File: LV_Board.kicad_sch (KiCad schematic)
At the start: 19 parts

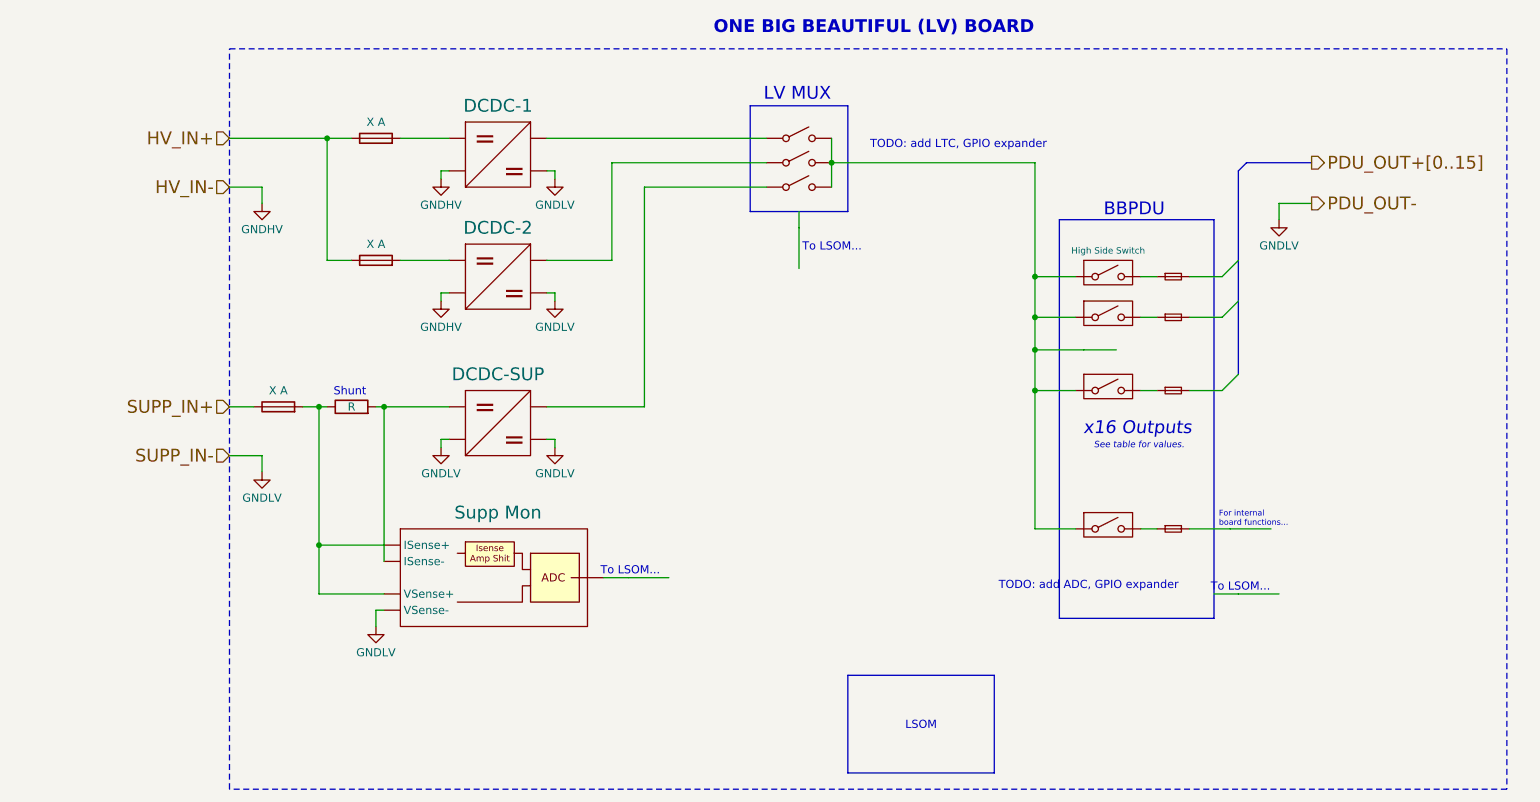
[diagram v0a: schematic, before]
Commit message: reorganized top
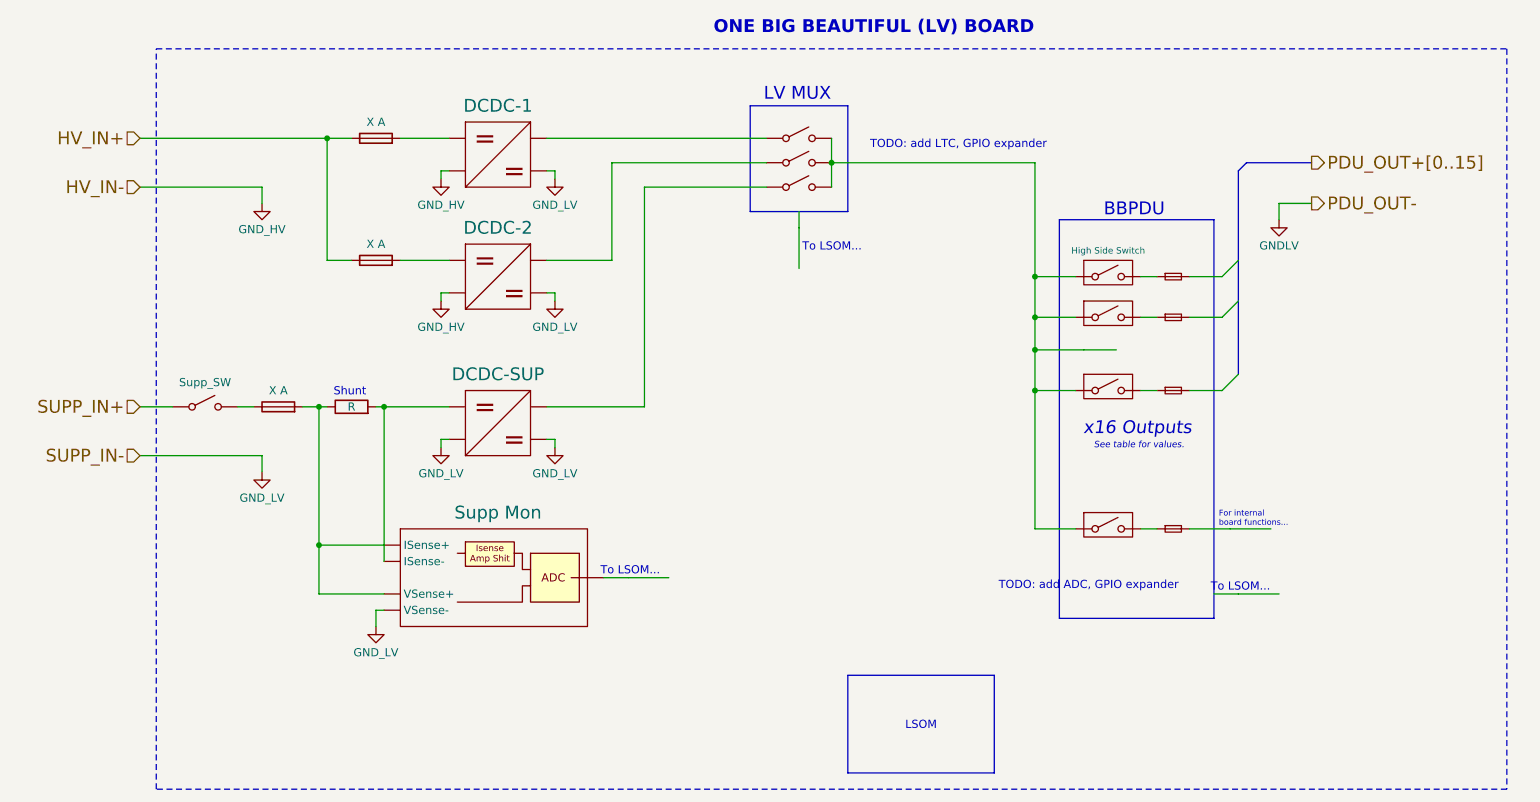
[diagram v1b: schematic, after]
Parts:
- added SW1: Supp_SW, symbol Switch:SW_SPST
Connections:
- net GNDHV is gone; now on net GND_LV: U?., U?.
- net GNDLV: no longer U?., U?., U?., U?.
- net SUPP_IN+: now also SW1. (B); no longer F?.1
- net GND_LV: now reaches U?.
- net GND_LV: now also U?.
- net at SW?. (B): now also SW?. (B), SW?. (B), U?., U?., U?., U?.; no longer U?.
- new net: R?.2, U?., U?.
- new net: SW?. (B), U?.
- new net: F?.1, SW1. (B)
- new net GND_HV: U?., U?.
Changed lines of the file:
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@@
 	(paper "A4")
 	(rectangle
-		(start 49.53 35.56)
+		(start 38.1 35.56)
 		(end 248.92 151.13)
 		(stroke
@@
 	(wire
 		(pts
-			(xy 49.53 91.44) (xy 53.34 91.44)
+			(xy 35.56 91.44) (xy 40.64 91.44)
 		)
 		(stroke
@@
 	(wire
 		(pts
-			(xy 49.53 57.15) (xy 54.61 57.15)
+			(xy 35.56 57.15) (xy 54.61 57.15)
 		)
 		(stroke
@@
 	(wire
 		(pts
+			(xy 50.8 91.44) (xy 53.34 91.44)
+		)
+		(stroke
+			(width 0)
+			(type default)
+		)
+	)
+	(wire
+		(pts
 			(xy 82.55 96.52) (xy 83.82 96.52)
 		)
@@
 	(wire
 		(pts
-			(xy 49.53 99.06) (xy 54.61 99.06)
+			(xy 35.56 99.06) (xy 54.61 99.06)
 		)
 		(stroke
@@
 	(wire
 		(pts
-			(xy 49.53 49.53) (xy 64.77 49.53)
+			(xy 35.56 49.53) (xy 64.77 49.53)
 		)
 		(stroke
@@
 			)
 		)
+		(column_widths 16.51 12.7)
+		(row_heights 2.54 2.54 2.54)
+		(cells
+			(table_cell "SIGNALS FROM"
+				(exclude_from_sim no)
+				(at 106.68 119.38 0)
+				(size 16.51 2.54)
+				(margins 0.9525 0.9525 0.9525 0.9525)
+				(span 1 1)
+				(fill
+					(type none)
+				)
+				(effects
+					(font
+						(size 1.27 1.27)
+						(thickness 0.254)
+						(bold yes)
+					)
+					(justify left top)
+				)
+			)
+			(table_cell "MEDIUM"
+				(exclude_from_sim no)
+				(at 123.19 119.38 0)
+				(size 12.7 2.54)
+				(margins 0.9525 0.9525 0.9525 0.9525)
+				(span 1 1)
+				(fill
+					(type none)
+				)
+				(effects
+					(font
+						(size 1.27 1.27)
+						(thickness 0.254)
+						(bold yes)
+					)
+					(justify left top)
+				)
+			)
+			(table_cell "VSense"
+				(exclude_from_sim no)
+				(at 106.68 121.92 0)
+				(size 16.51 2.54)
+				(margins 0.9525 0.9525 0.9525 0.9525)
+				(span 1 1)
+				(fill
+					(type none)
+				)
+				(effects
+					(font
+						(size 1 1)
+					)
+					(justify left top)
+				)
+			)
+			(table_cell "SPI ADC"
+				(exclude_from_sim no)
+				(at 123.19 121.92 0)
+				(size 12.7 2.54)
+				(margins 0.9525 0.9525 0.9525 0.9525)
+				(span 1 1)
+				(fill
+					(type none)
+				)
+				(effects
+					(font
+						(size 1 1)
+					)
+					(justify left top)
+				)
+			)
+			(table_cell "ISense"
+				(exclude_from_sim no)
+				(at 106.68 124.46 0)
+				(size 16.51 2.54)
+				(margins 0.9525 0.9525 0.9525 0.9525)
+				(span 1 1)
+				(fill
+					(type none)
+				)
+				(effects
+					(font
+						(size 1 1)
+					)
+					(justify left top)
+				)
+			)
+			(table_cell "SPI ADC"
+				(exclude_from_sim no)
+				(at 123.19 124.46 0)
+				(size 12.7 2.54)
+				(margins 0.9525 0.9525 0.9525 0.9525)
+				(span 1 1)
+				(fill
+					(type none)
+				)
+				(effects
+					(font
+						(size 1 1)
+					)
+					(justify left top)
+				)
+			)
+		)
+	)
+	(table
+		(column_count 2)
+		(border
+			(external yes)
+			(header yes)
+			(stroke
+				(width 0)
+				(type solid)
+			)
+		)
+		(separators
+			(rows yes)
+			(cols yes)
+			(stroke
+				(width 0)
+				(type solid)
+			)
+		)
 		(column_widths 22.86 12.7)
 		(row_heights 2.54 2.54 2.54 2.54 2.54 2.54 2.54 2.54 2.54 2.54)
@@
 		)
 	)
-	(table
-		(column_count 2)
-		(border
-			(external yes)
-			(header yes)
-			(stroke
-				(width 0)
-				(type solid)
-			)
-		)
-		(separators
-			(rows yes)
-			(cols yes)
-			(stroke
-				(width 0)
-				(type solid)
-			)
-		)
-		(column_widths 16.51 12.7)
-		(row_heights 2.54 2.54 2.54)
-		(cells
-			(table_cell "SIGNALS FROM"
-				(exclude_from_sim no)
-				(at 106.68 119.38 0)
-				(size 16.51 2.54)
-				(margins 0.9525 0.9525 0.9525 0.9525)
-				(span 1 1)
-				(fill
-					(type none)
-				)
-				(effects
-					(font
-						(size 1.27 1.27)
-						(thickness 0.254)
-						(bold yes)
-					)
-					(justify left top)
-				)
-			)
-			(table_cell "MEDIUM"
-				(exclude_from_sim no)
-				(at 123.19 119.38 0)
-				(size 12.7 2.54)
-				(margins 0.9525 0.9525 0.9525 0.9525)
-				(span 1 1)
-				(fill
-					(type none)
-				)
-				(effects
-					(font
-						(size 1.27 1.27)
-						(thickness 0.254)
-						(bold yes)
-					)
-					(justify left top)
-				)
-			)
-			(table_cell "VSense"
-				(exclude_from_sim no)
-				(at 106.68 121.92 0)
-				(size 16.51 2.54)
-				(margins 0.9525 0.9525 0.9525 0.9525)
-				(span 1 1)
-				(fill
-					(type none)
-				)
-				(effects
-					(font
-						(size 1 1)
-					)
-					(justify left top)
-				)
-			)
-			(table_cell "SPI ADC"
-				(exclude_from_sim no)
-				(at 123.19 121.92 0)
-				(size 12.7 2.54)
-				(margins 0.9525 0.9525 0.9525 0.9525)
-				(span 1 1)
-				(fill
-					(type none)
-				)
-				(effects
-					(font
-						(size 1 1)
-					)
-					(justify left top)
-				)
-			)
-			(table_cell "ISense"
-				(exclude_from_sim no)
-				(at 106.68 124.46 0)
-				(size 16.51 2.54)
-				(margins 0.9525 0.9525 0.9525 0.9525)
-				(span 1 1)
-				(fill
-					(type none)
-				)
-				(effects
-					(font
-						(size 1 1)
-					)
-					(justify left top)
-				)
-			)
-			(table_cell "SPI ADC"
-				(exclude_from_sim no)
-				(at 123.19 124.46 0)
-				(size 12.7 2.54)
-				(margins 0.9525 0.9525 0.9525 0.9525)
-				(span 1 1)
-				(fill
-					(type none)
-				)
-				(effects
-					(font
-						(size 1 1)
-					)
-					(justify left top)
-				)
-			)
-		)
-	)
 	(hierarchical_label "HV_IN-"
 		(shape input)
-		(at 49.53 57.15 180)
+		(at 35.56 57.15 180)
 		(effects
 			(font
@@
 	(hierarchical_label "HV_IN+"
 		(shape input)
-		(at 49.53 49.53 180)
+		(at 35.56 49.53 180)
 		(effects
 			(font
@@
 	(hierarchical_label "SUPP_IN-"
 		(shape input)
-		(at 49.53 99.06 180)
+		(at 35.56 99.06 180)
 		(effects
 			(font
@@
 	(hierarchical_label "SUPP_IN+"
 		(shape input)
-		(at 49.53 91.44 180)
+		(at 35.56 91.44 180)
 		(effects
 			(font
@@
 			)
 		)
-		(property "Value" "GNDLV"
+		(property "Value" "GND_LV"
 			(at 100.33 78.994 0)
 			(effects
@@
 			)
 		)
-		(property "Value" "GNDHV"
+		(property "Value" "GND_HV"
 			(at 54.61 63.754 0)
 			(effects
@@
 			)
 		)
-		(property "Value" "GNDLV"
+		(property "Value" "GND_LV"
 			(at 72.39 129.794 0)
 			(effects
@@
 			)
 		)
-		(property "Value" "GNDLV"
+		(property "Value" "GND_LV"
 			(at 100.33 59.944 0)
 			(effects
@@
 			)
 		)
-		(property "Value" "GNDLV"
+		(property "Value" "GND_LV"
 			(at 82.55 101.854 0)
 			(effects
@@
 	)
 	(symbol
+		(lib_name "SW_SPST_4")
+		(lib_id "Switch:SW_SPST")
+		(at 45.72 91.44 0)
+		(unit 1)
+		(exclude_from_sim no)
+		(in_bom yes)
+		(on_board yes)
+		(dnp no)
+		(fields_autoplaced yes)
+		(property "Reference" "SW1"
+			(at 45.72 85.09 0)
+			(effects
+				(font
+					(size 1.27 1.27)
+				)
+				(hide yes)
+			)
+		)
+		(property "Value" "Supp_SW"
+			(at 45.72 87.63 0)
+			(effects
+				(font
+					(size 1.27 1.27)
+				)
+			)
+		)
+		(property "Footprint" ""
+			(at 45.72 91.44 0)
+			(effects
+				(font
+					(size 1.27 1.27)
+				)
+				(hide yes)
+			)
+		)
+		(property "Datasheet" "~"
+			(at 45.72 91.44 0)
+			(effects
+				(font
+					(size 1.27 1.27)
+				)
+				(hide yes)
+			)
+		)
+		(property "Description" "Single Pole Single Throw (SPST) switch"
+			(at 45.72 91.44 0)
+			(effects
+				(font
+					(size 1.27 1.27)
+				)
+				(hide yes)
+			)
+		)
+		(pin ""
+		)
+		(pin ""
+		)
+		(instances
+			(project "ElectricalSystem"
+				(path "/7dc721ab-4b7a-42e7-8fa4-f406a2ddcd46/e706363e-1a72-498a-80b9-68cba960c42a"
+					(reference "SW1")
+					(unit 1)
+				)
+			)
+		)
+	)
+	(symbol
 		(lib_id "power:GND")
 		(at 100.33 97.79 0)
@@
 			)
 		)
-		(property "Value" "GNDLV"
+		(property "Value" "GND_LV"
 			(at 100.33 101.854 0)
 			(effects
@@
 			)
 		)
-		(property "Value" "GNDLV"
+		(property "Value" "GND_LV"
 			(at 54.61 105.664 0)
 			(effects
@@
 			)
 		)
-		(property "Value" "GNDHV"
+		(property "Value" "GND_HV"
 			(at 82.55 78.994 0)
 			(effects
@@
 			)
 		)
-		(property "Value" "GNDHV"
+		(property "Value" "GND_HV"
 			(at 82.55 59.944 0)
 			(effects
